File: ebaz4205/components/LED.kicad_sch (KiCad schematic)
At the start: 1 part

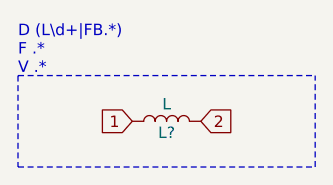
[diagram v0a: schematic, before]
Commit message: Provided all component symbols.
Symbol libraries are available as subdirectories in ebaz4205/components/

U23 is still unknown, so a placeholder symbol was provided.
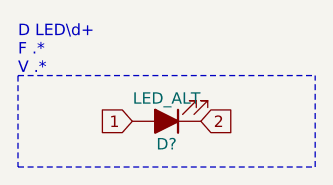
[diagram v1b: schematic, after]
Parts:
- removed L?: L, symbol Device:L
- added D?: LED_ALT, symbol Device:LED_ALT
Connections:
- net 1: now also D?.2 (A)
- net 2: now also D?.1 (K)
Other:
- note added: "D LED\d+ F .* V .*"
- note removed: "D (L\d+|FB.*) F .* V .*"
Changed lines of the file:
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@@
     (stroke (width 0) (type dash) (color 0 0 0 0))
   )
-  (text "D (L\\d+|FB.*)\nF .*\nV .*" (at 0 0 0)
+  (text "D LED\\d+\nF .*\nV .*" (at 0 0 0)
     (effects (font (size 1.27 1.27)) (justify left bottom))
   )
@@
     (effects (font (size 1.27 1.27)) (justify left))
   )
-  (symbol (lib_id "Device:L") (at 16.51 5.08 90) (unit 1)
+  (symbol (lib_id "Device:LED_ALT") (at 16.51 5.08 180) (unit 1)
     (in_bom yes) (on_board yes)
-    (property "Reference" "L?" (id 0) (at 16.51 6.35 90))
-    (property "Value" "L" (id 1) (at 16.51 3.175 90))
+    (property "Reference" "D?" (id 0) (at 16.51 7.62 0))
+    (property "Value" "LED_ALT" (id 1) (at 16.51 2.54 0))
     (property "Footprint" "" (id 2) (at 16.51 5.08 0)
       (effects (font (size 1.27 1.27)) hide)
@@
   )
   (symbol_instances
-    (path "/c384dce7-3587-4a56-b341-110e41afcf1c"
-      (reference "L?") (unit 1) (value "L") (footprint "")
+    (path "/1df90115-e60d-444f-82df-be57494625d5"
+      (reference "D?") (unit 1) (value "LED_ALT") (footprint "")
     )
   )
